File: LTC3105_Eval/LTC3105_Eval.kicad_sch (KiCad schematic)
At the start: 13 parts, among them J1 Conn_01x05_Pin, J2 Conn_01x05_Pin, U1 LTC3105EMS

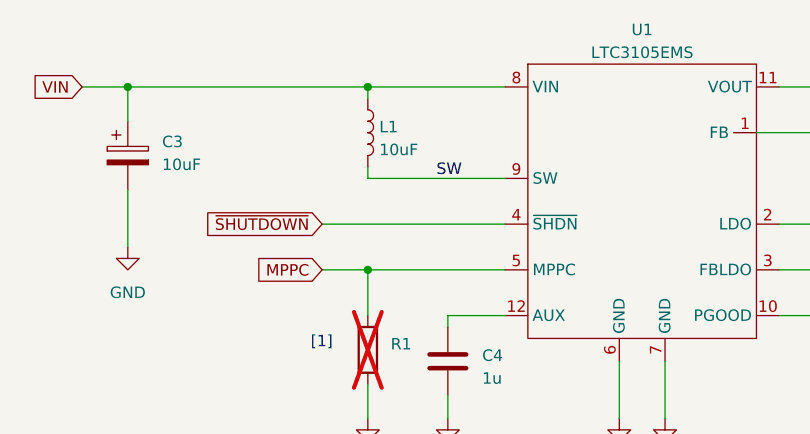
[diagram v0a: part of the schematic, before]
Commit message: resolved #8, #7, #6 and #5 ; closed #5 and #3
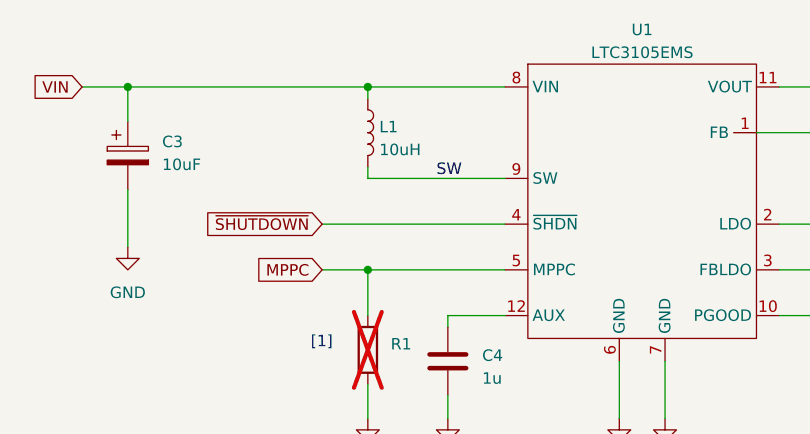
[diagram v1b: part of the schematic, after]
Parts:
- C1, C3: footprint Capacitor_Tantalum_SMD:CP_EIA-6032-28_Kemet-C -> Capacitor_Tantalum_SMD:CP_EIA-3216-18_Kemet-A_Pad1.58x1.35mm_HandSolder; dist no 74-293D106X9025C2TE3 -> 581-TAJA106K006SNJ; man Vishay -> KYOCERA AVX; man no 293D106X9025C2TE3 -> TAJA106K006SNJ
- L1: value 10uF -> 10uH; footprint Inductor_SMD:L_Coilcraft_LPS4018 -> 021_inductor:L_Coilcraft_MSS5131-XXX_handsolder
- R1, R2, R3, R4, R5: footprint Resistor_SMD:R_0805_2012Metric -> Resistor_SMD:R_0603_1608Metric_Pad0.98x0.95mm_HandSolder
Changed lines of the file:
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@@
 	(title_block
 		(title "LTC3105 Evaluation Board")
-		(date "2024-06-23")
-		(rev "V0.0.0")
+		(date "2024-12-30")
+		(rev "V1.0.0")
 		(company "© Edwin Koch 2024, This work is licenced under CERN-OHL-P V 2.0.")
 	)
@@
 			)
 		)
-		(property "Footprint" "Resistor_SMD:R_0805_2012Metric"
+		(property "Footprint" "Resistor_SMD:R_0603_1608Metric_Pad0.98x0.95mm_HandSolder"
 			(at 225.552 55.88 90)
 			(effects
@@
 			)
 		)
-		(property "Value" "10uF"
+		(property "Value" "10uH"
 			(at 100.33 56.515 0)
 			(effects
@@
 			)
 		)
-		(property "Footprint" "Inductor_SMD:L_Coilcraft_LPS4018"
+		(property "Footprint" "021_inductor:L_Coilcraft_MSS5131-XXX_handsolder"
 			(at 99.06 54.61 0)
 			(effects
@@
 			)
 		)
-		(property "Footprint" "Capacitor_Tantalum_SMD:CP_EIA-6032-28_Kemet-C"
+		(property "Footprint" "Capacitor_Tantalum_SMD:CP_EIA-3216-18_Kemet-A_Pad1.58x1.35mm_HandSolder"
 			(at 73.3552 60.96 0)
 			(effects
@@
 			)
 		)
-		(property "Datasheet" "https://www.vishay.com/doc?40002"
+		(property "Datasheet" "http://datasheets.kyocera-avx.com/TAJ.pdf"
 			(at 72.39 57.15 0)
 			(effects
@@
 			)
 		)
-		(property "dist no" "74-293D106X9025C2TE3 "
+		(property "dist no" "581-TAJA106K006SNJ "
 			(at 72.39 57.15 0)
 			(effects
@@
 			)
 		)
-		(property "man" "Vishay"
+		(property "man" "KYOCERA AVX "
 			(at 72.39 57.15 0)
 			(effects
@@
 			)
 		)
-		(property "man no" "293D106X9025C2TE3 "
+		(property "man no" "TAJA106K006SNJ"
 			(at 72.39 57.15 0)
 			(effects
@@
 			)
 		)
-		(property "Footprint" "Resistor_SMD:R_0805_2012Metric"
+		(property "Footprint" "Resistor_SMD:R_0603_1608Metric_Pad0.98x0.95mm_HandSolder"
 			(at 97.282 78.74 90)
 			(effects
@@
 			)
 		)
-		(property "Footprint" "Resistor_SMD:R_0805_2012Metric"
+		(property "Footprint" "Resistor_SMD:R_0603_1608Metric_Pad0.98x0.95mm_HandSolder"
 			(at 174.752 80.01 90)
 			(effects
@@
 			)
 		)
-		(property "Footprint" "Capacitor_Tantalum_SMD:CP_EIA-6032-28_Kemet-C"
+		(property "Footprint" "Capacitor_Tantalum_SMD:CP_EIA-3216-18_Kemet-A_Pad1.58x1.35mm_HandSolder"
 			(at 254.9652 68.58 0)
 			(effects
@@
 			)
 		)
-		(property "Datasheet" "https://www.vishay.com/doc?40002"
+		(property "Datasheet" "http://datasheets.kyocera-avx.com/TAJ.pdf"
 			(at 254 64.77 0)
 			(effects
@@
 			)
 		)
-		(property "dist no" "74-293D106X9025C2TE3 "
+		(property "dist no" "581-TAJA106K006SNJ "
 			(at 254 64.77 0)
 			(effects
@@
 			)
 		)
-		(property "man" "Vishay"
+		(property "man" "KYOCERA AVX "
 			(at 254 64.77 0)
 			(effects
@@
 			)
 		)
-		(property "man no" "293D106X9025C2TE3 "
+		(property "man no" "TAJA106K006SNJ"
 			(at 254 64.77 0)
 			(effects
@@
 			)
 		)
-		(property "Footprint" "Resistor_SMD:R_0805_2012Metric"
+		(property "Footprint" "Resistor_SMD:R_0603_1608Metric_Pad0.98x0.95mm_HandSolder"
 			(at 174.752 91.44 90)
 			(effects
@@
 			)
 		)
-		(property "Footprint" "Resistor_SMD:R_0805_2012Metric"
+		(property "Footprint" "Resistor_SMD:R_0603_1608Metric_Pad0.98x0.95mm_HandSolder"
 			(at 225.552 68.58 90)
 			(effects
